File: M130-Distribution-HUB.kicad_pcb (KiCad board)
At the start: 4 copper layers, 152.4 x 114.3 mm, 23 parts, among them CN0 6437288-3

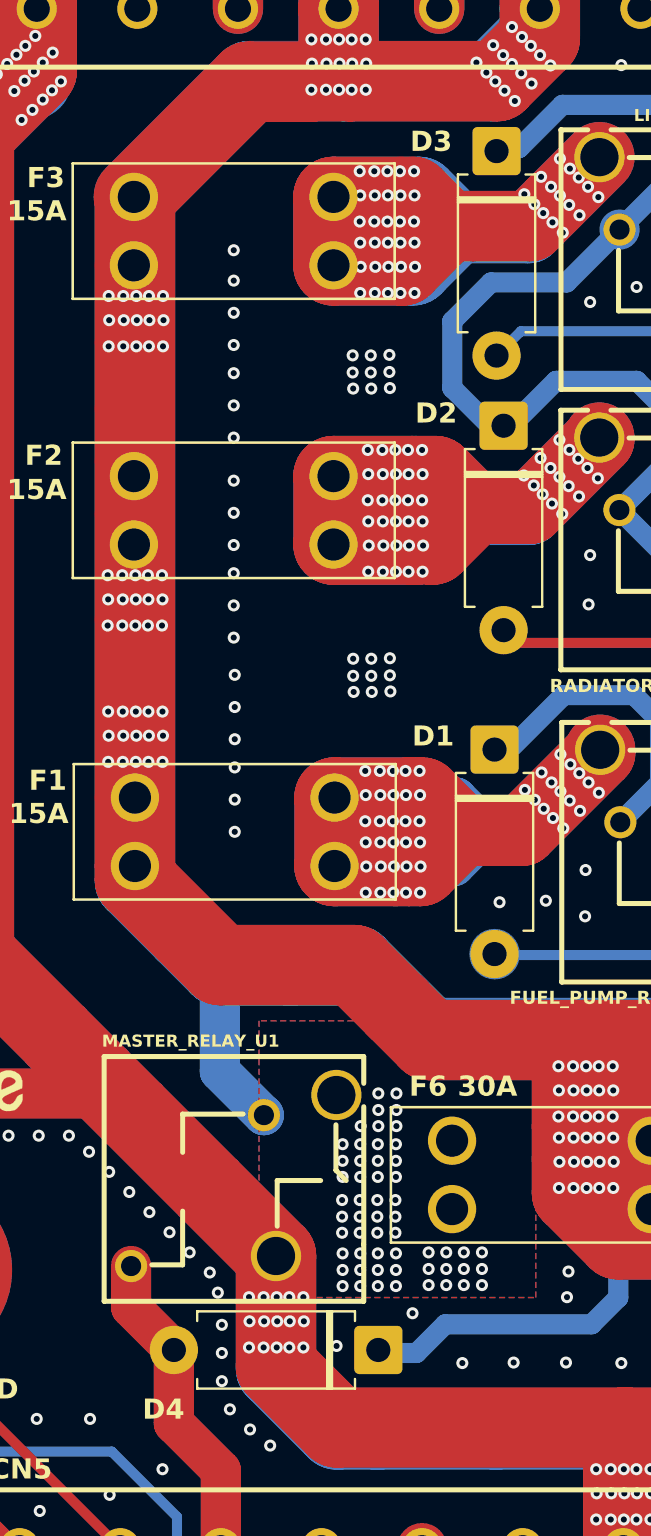
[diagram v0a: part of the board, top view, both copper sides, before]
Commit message: Stich via adjustments
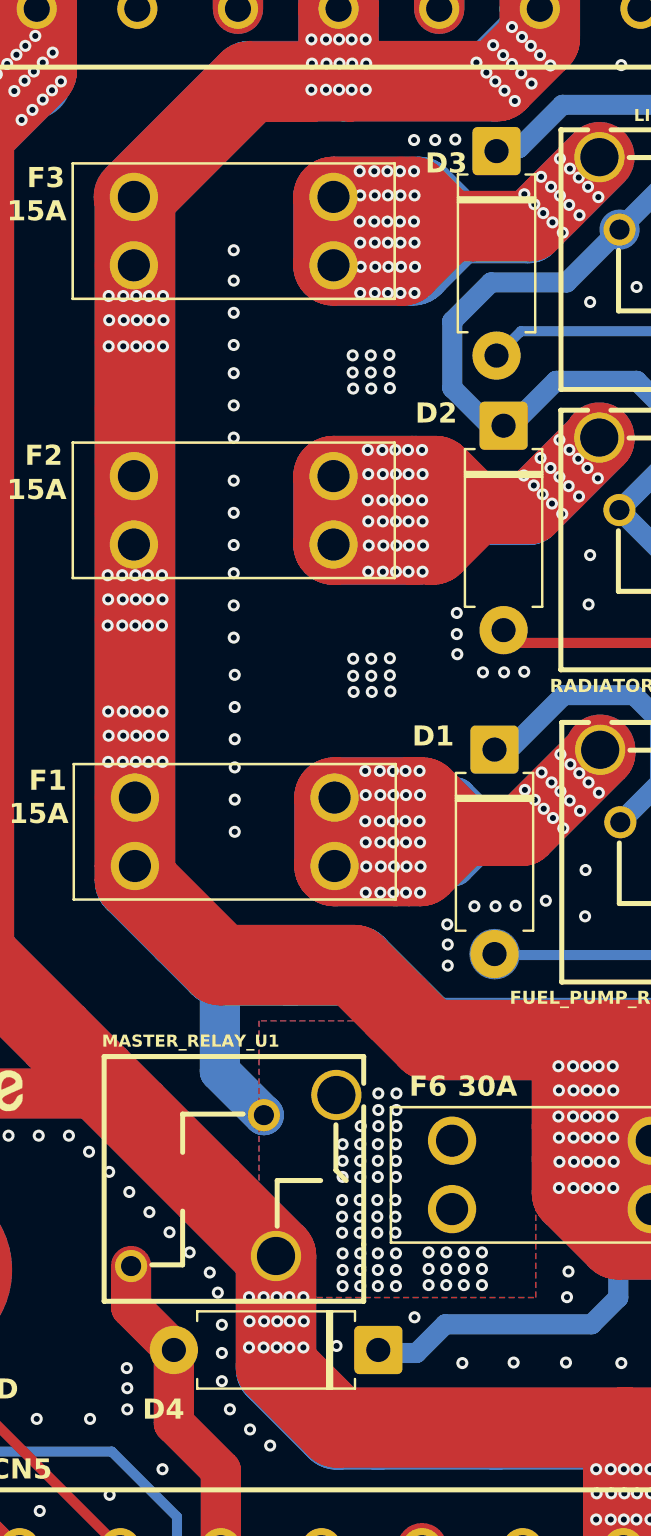
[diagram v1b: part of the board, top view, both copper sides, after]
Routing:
- net GND: vias 912 -> 929

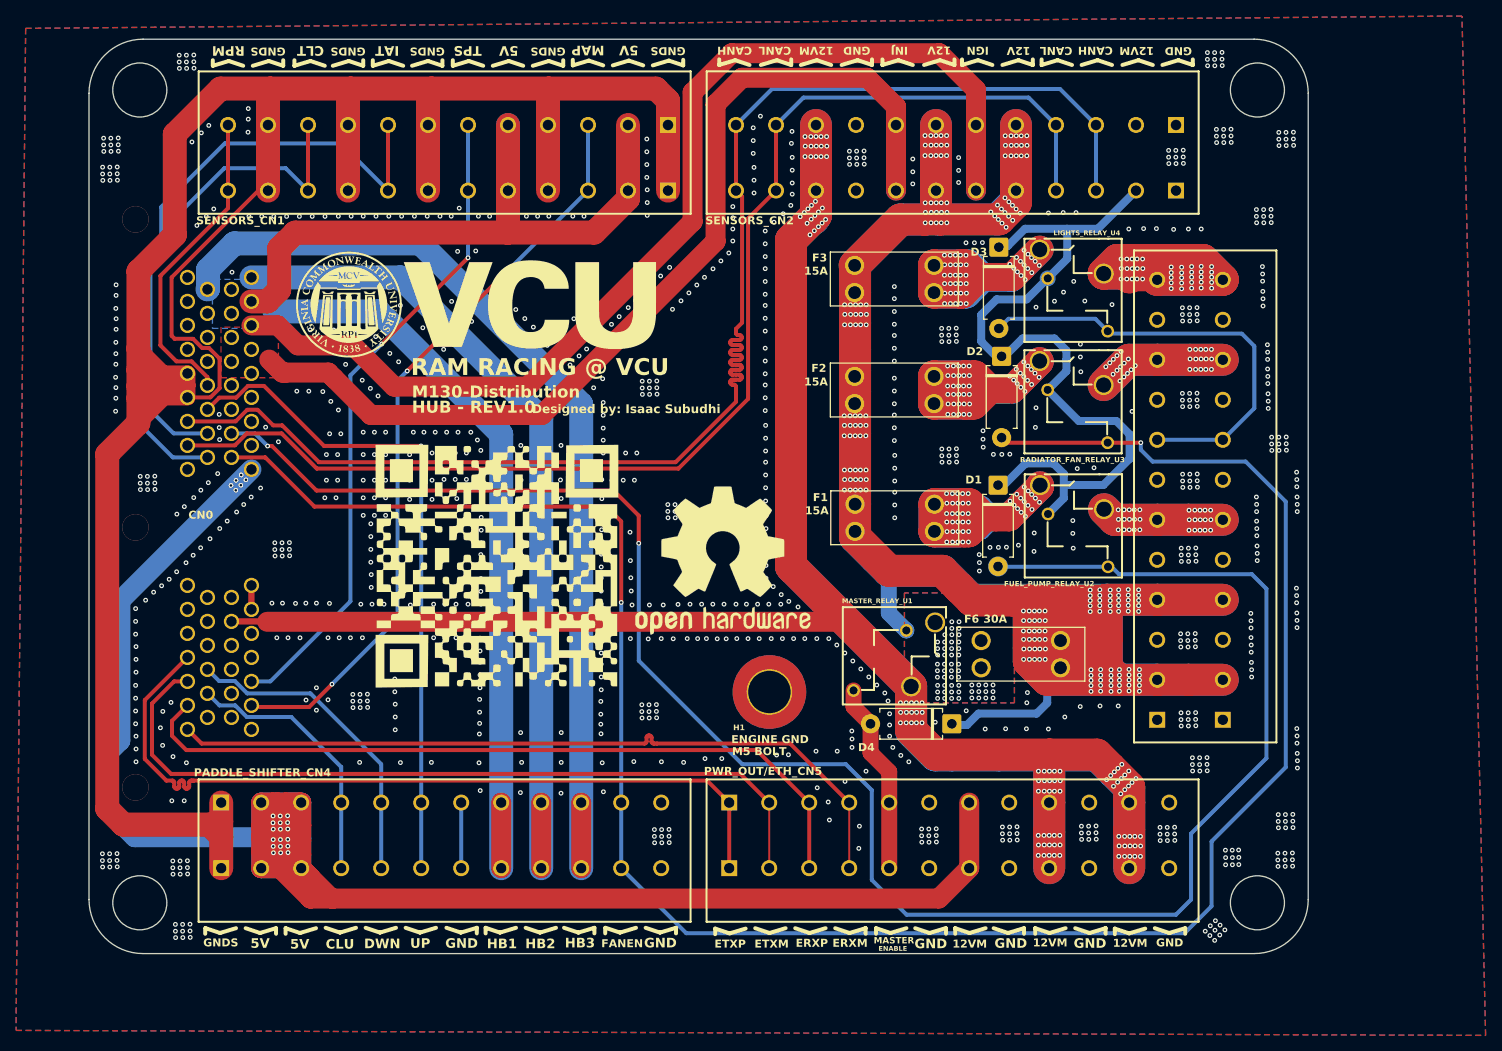
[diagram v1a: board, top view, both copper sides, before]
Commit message: Thermal relif
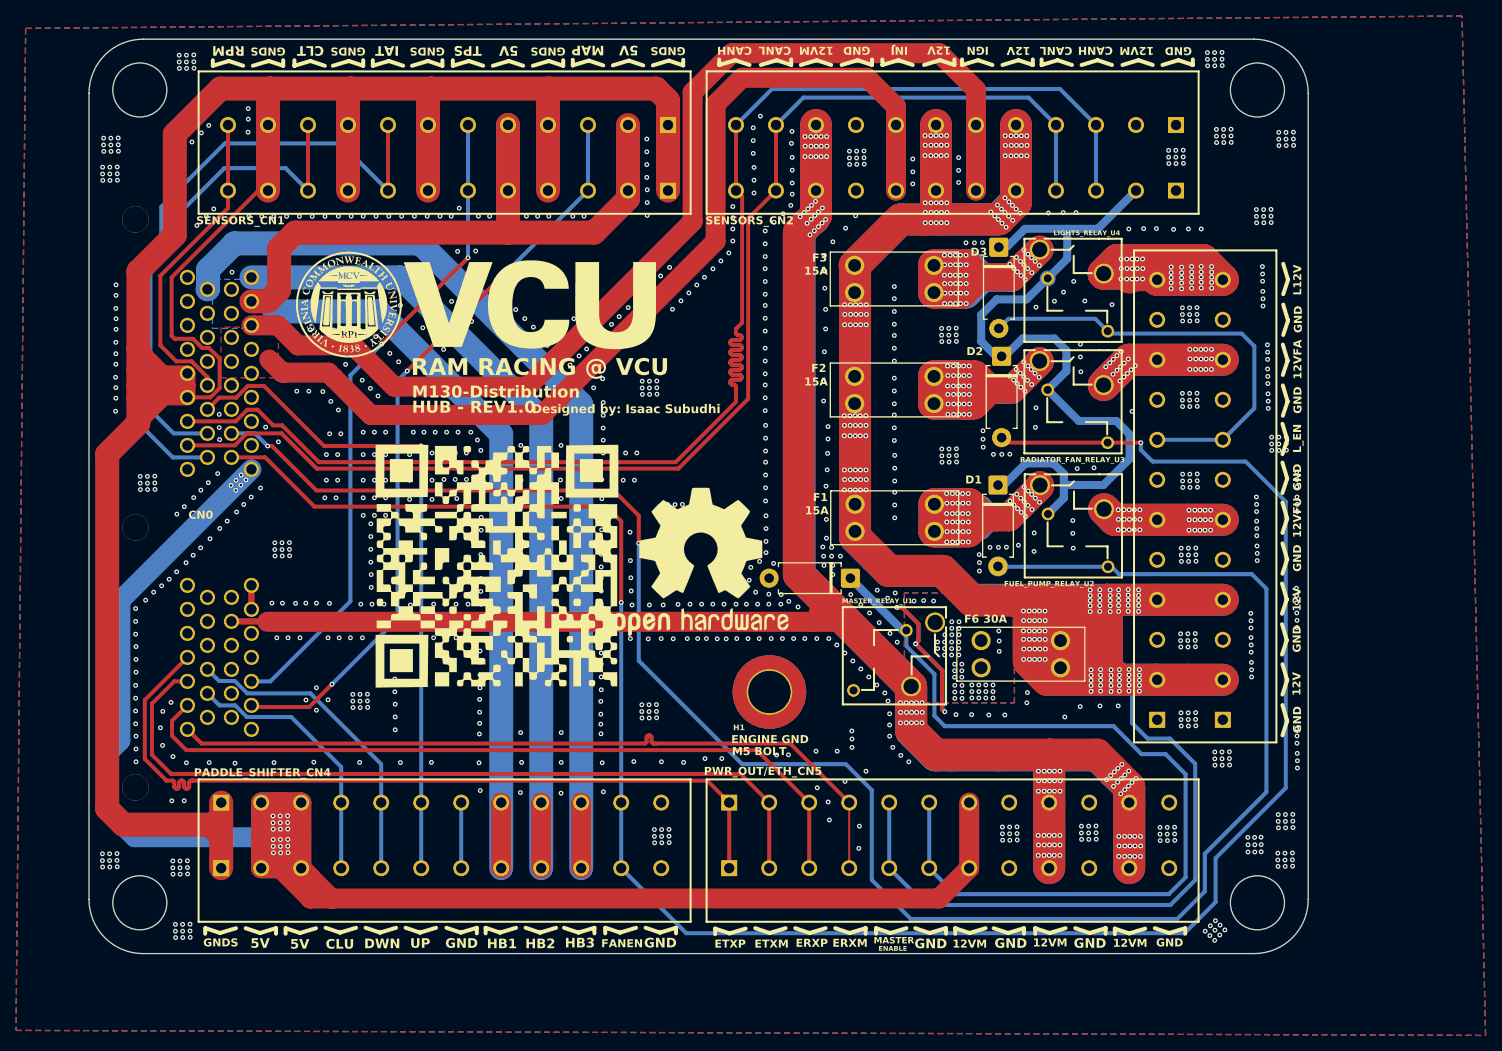
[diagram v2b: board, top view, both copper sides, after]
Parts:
- moved D4 22.2 mm to (155.5, 105.8)
- moved REF** 2.76 mm to (136.8, 103.8)
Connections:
- D4 pad 1: /12V_BATT -> /MASTER_RELAY_EN
- D4 pad 2: /MASTER_RELAY_EN -> GND
- MASTER_RELAY_U1 pad 1: /12V_BATT -> /MASTER_RELAY_EN
- MASTER_RELAY_U1 pad 2: /MASTER_RELAY_EN -> GND
- PWR_OUT/ETH_CN5 pad 5: /MASTER_RELAY_EN -> /12V_BATT
- PWR_OUT/ETH_CN5 pad 6: GND -> /MASTER_RELAY_EN
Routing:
- net /MASTER_RELAY_EN: track 24.1 -> 112.1 mm
- net GND: track 11.6 -> 76.3 mm, vias 929 -> 963
- net /12V_BATT: track 844.5 -> 899.8 mm
- net /A23-INJ_LS1: track 240.6 -> 241.5 mm
- net /12V_OUT_MASTER_RELAY: track 806.2 -> 806.8 mm
- net /MASTER_FUSE_OUT: vias 55 -> 48
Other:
- board text added: "12VFA"
- board text added: "12VFU"
- board text added: "L12V"
- board text added: "L_EN"

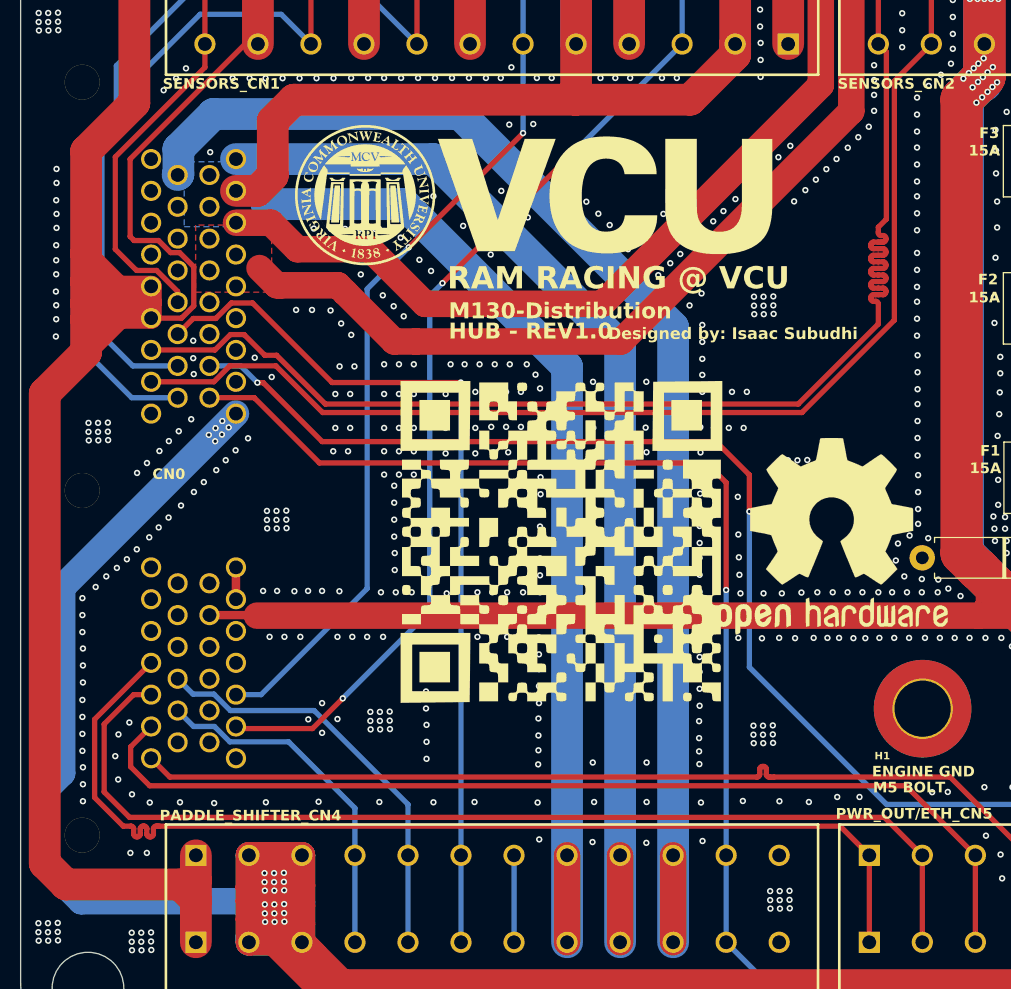
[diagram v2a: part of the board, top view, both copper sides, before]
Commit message: Fixed DRC issues.
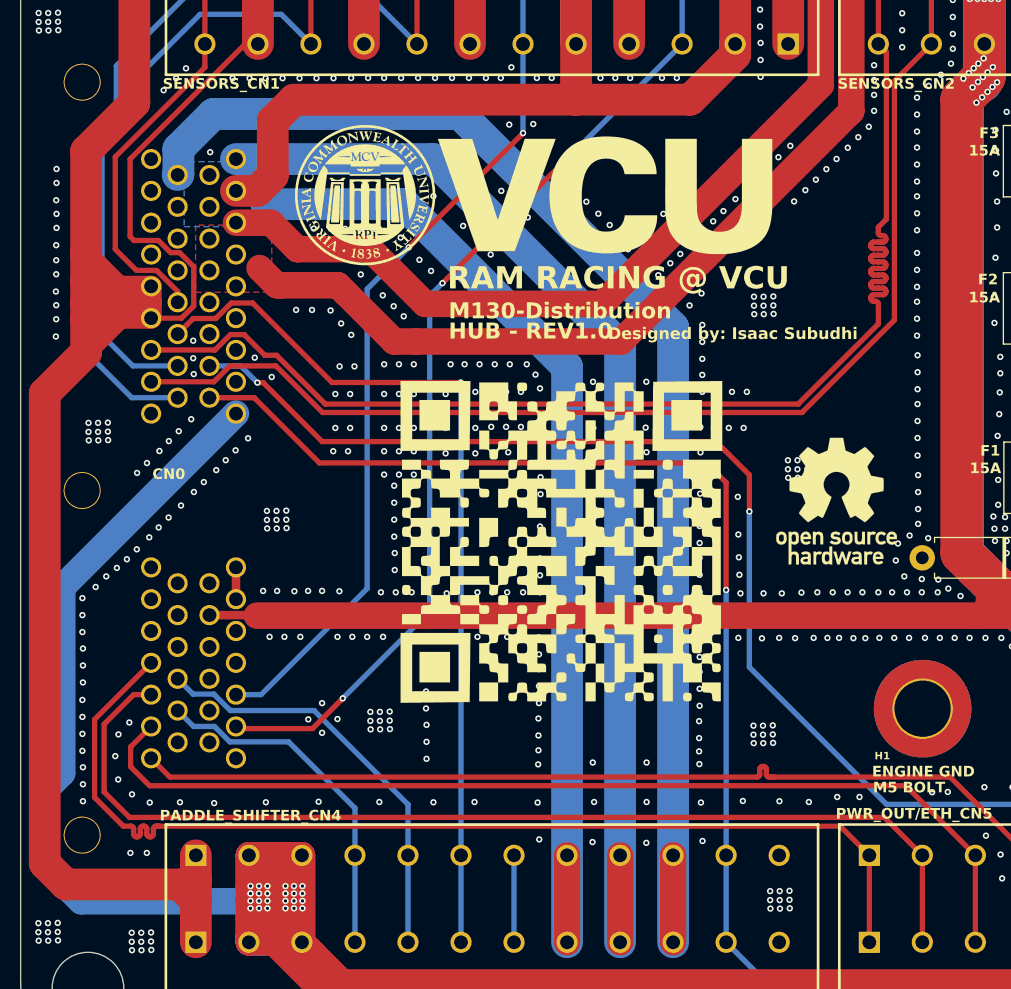
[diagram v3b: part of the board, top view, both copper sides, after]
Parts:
- removed the REF** at (136.8, 103.8)
- removed the REF** at (131.1, 67.0)
- added REF**: OSHW-Logo_11.4x12mm_SilkScreen, Symbol:OSHW-Logo_11.4x12mm_SilkScreen, F.Cu at (137.2, 100.5)
- added REF**: OSHW-Logo_11.4x12mm_SilkScreen, Symbol:OSHW-Logo_11.4x12mm_SilkScreen, B.Cu at (134.0, 66.2)
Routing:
- net GND: vias 963 -> 939
- net /A09-SEN_5V0_B: vias 0 -> 24
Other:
- board text added: "12V ALTERN"
- board text added: "12V BATT"
- board text added: "12V FAN"
- board text added: "12V FUEL"
- board text added: "12V LIGHTS"
- board text added: "LIGHTS EN"

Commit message: Moved to vertical connectors
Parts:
- PADDLE_SHIFTER_CN4, PWR_IN/RELAY_CN3, PWR_OUT/ETH_CN5, SENSORS_CN1, SENSORS_CN2: value 1190310 -> 1991192; footprint EasyEDA:CONN-TH_12P-P5.00_1190310 -> EasyEDA:PHOENIX_1991192
- moved PWR_IN/RELAY_CN3 30.6 mm to (204.6, 125.9)
- moved PADDLE_SHIFTER_CN4 30.5 mm to (74.5, 144.7)
- moved SENSORS_CN2 30.5 mm to (198.5, 46.6)
- moved SENSORS_CN1 30.5 mm to (135.0, 46.6)
- moved PWR_OUT/ETH_CN5 30.5 mm to (138.1, 144.7)
- moved RADIATOR_FAN_RELAY_U3 0.10 mm to (183.4, 83.9)
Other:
- board text added: "D4"
